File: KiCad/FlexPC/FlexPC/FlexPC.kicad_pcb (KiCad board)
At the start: 2 copper layers, 14.8 x 14.5 mm, 3 parts, among them J1 Conn_01x28, J2 Conn_01x20, J3 Conn_01x08

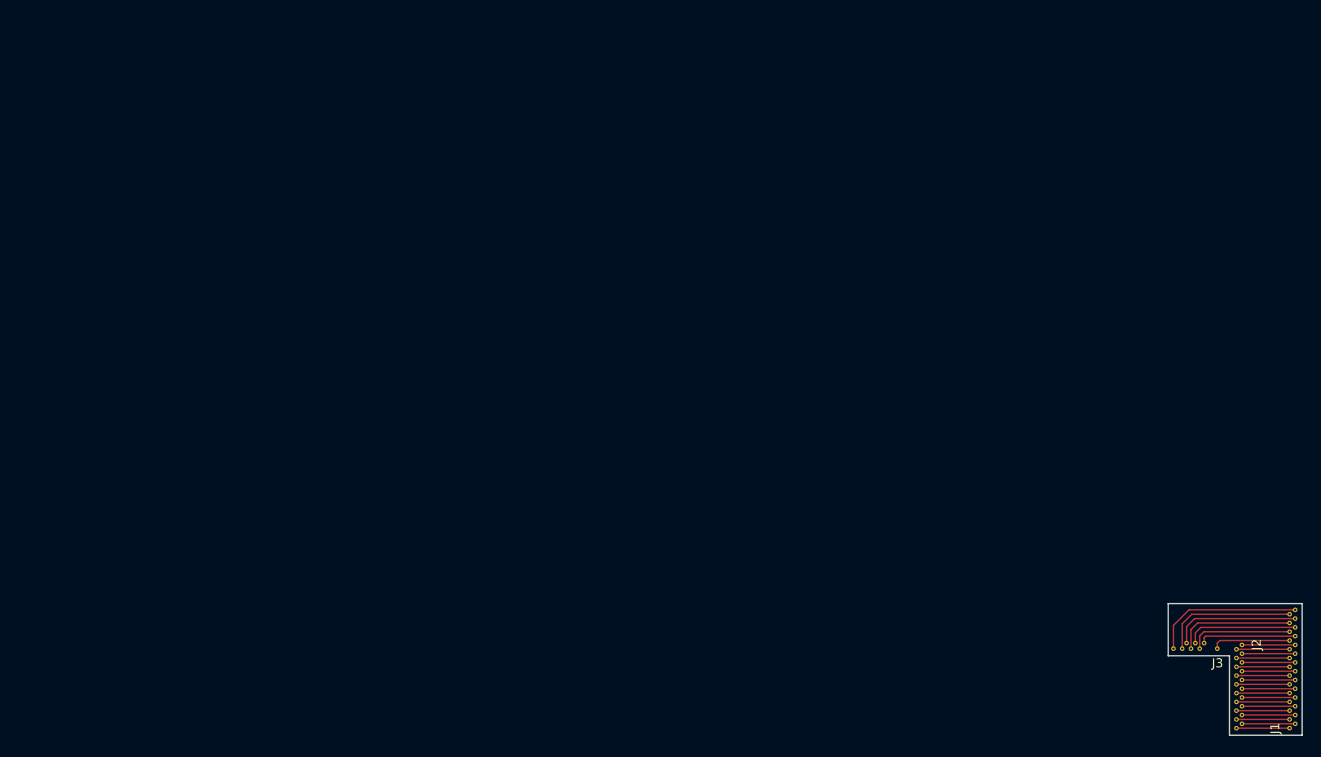
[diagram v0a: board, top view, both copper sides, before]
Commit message: FlexPC Cable
1. FlexPC Cable Generated
2. Via-trace distances are now 5 mils minimum
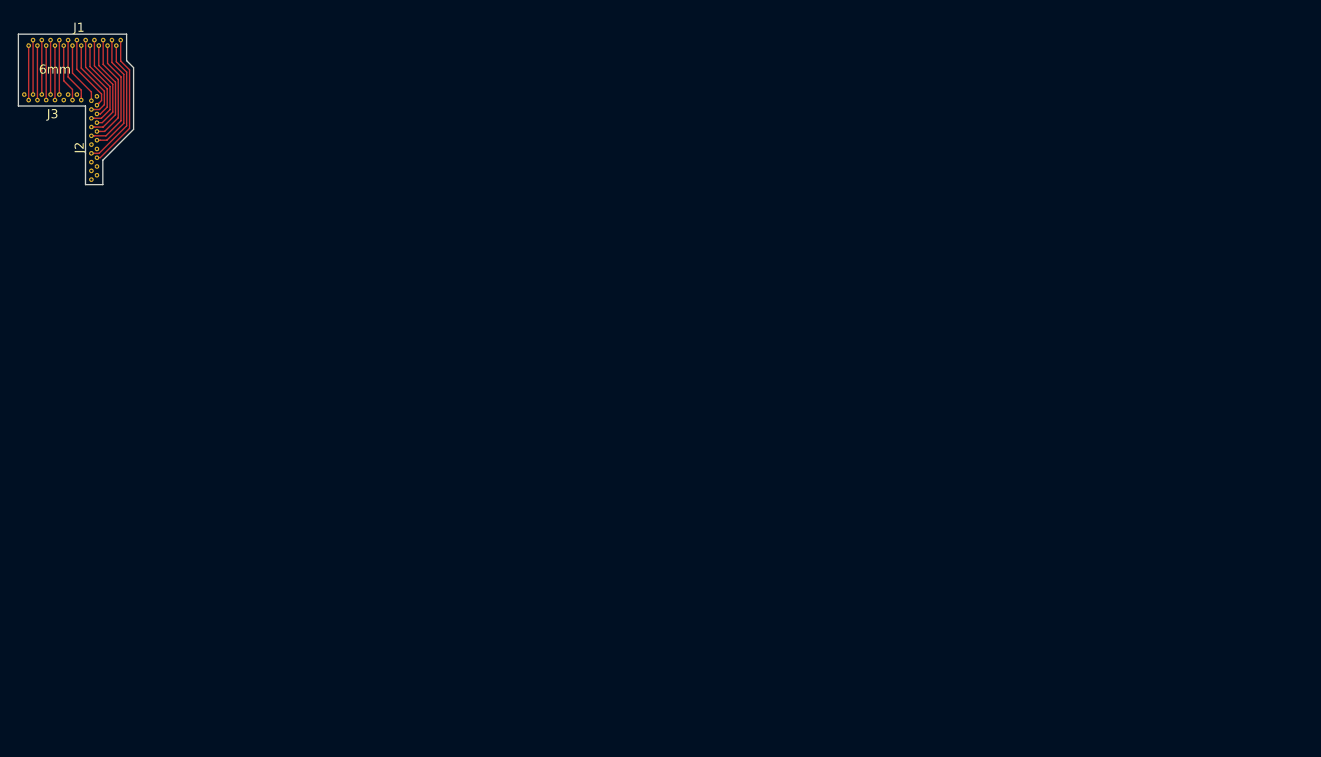
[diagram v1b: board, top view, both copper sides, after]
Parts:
- J1: value Conn_01x28 -> Conn_01x22; footprint .Connector:B2B_Flex_28_Dual_Row_38milx24mil_Hole_10milx20mil -> .Connector:B2B_Flex_22_Dual_Row_38milx24mil_Hole_10milx20mil
- J3: value Conn_01x08 -> Conn_01x14; footprint .Connector:B2B_Flex_08_Dual_Row_38milx24mil_Hole_10milx20mil -> .Connector:B2B_Flex_14_Dual_Row_38milx24mil_Hole_10milx20mil
- moved J1 149.4 mm to (37.9, 22.2), turned to 180 degrees
- moved J3 144.9 mm to (27.3, 28.2), turned to 0 degrees
- moved J2 139.8 mm to (35.3, 28.4)
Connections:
- J1 pad 1: Net-(J1-Pad1) -> /LINE_VALID
- J1 pad 10: /img_d7 -> /img_d2
- J1 pad 11: /img_d6 -> /img_d0
- J1 pad 12: Net-(J1-Pad12) -> /1V8
- J1 pad 13: Net-(J1-Pad13) -> /GND
- J1 pad 14: /FRAME_VALID -> /SS_N
- J1 pad 15: /LINE_VALID -> /SCK
- J1 pad 16: Net-(J1-Pad16) -> /RESET_N
- J1 pad 17: Net-(J1-Pad17) -> /TRIGGER0
- J1 pad 18: Net-(J1-Pad18) -> /MONITOR0
- J1 pad 19: Net-(J1-Pad19) -> /MISO
- J1 pad 2: Net-(J1-Pad2) -> /FRAME_VALID
- J1 pad 20: Net-(J1-Pad20) -> /MOSI
- J1 pad 21: /SS_N -> /3V3
- J1 pad 22: /SCK -> /Status_LED
- J1 pad 3: /img_d0 -> /img_d6
- J1 pad 4: /img_d2 -> /img_d7
- J1 pad 5: /img_d1 -> /img_d5
- J1 pad 6: /img_d3 -> /img_d4
- J1 pad 8: /img_d4 -> /img_d3
- J1 pad 9: /img_d5 -> /img_d1
- J2 pad 1: Net-(J1-Pad20) -> Net-(J2-Pad1)
- J2 pad 10: /img_d6 -> /img_d7
- J2 pad 11: /img_d7 -> /img_d6
- J2 pad 12: /img_d5 -> /img_d8
- J2 pad 13: /img_d4 -> /img_d9
- J2 pad 14: /CLK_OUT -> /FRAME_VALID
- J2 pad 15: /img_d3 -> /LINE_VALID
- J2 pad 16: /img_d1 -> Net-(J2-Pad16)
- J2 pad 17: /img_d2 -> Net-(J2-Pad17)
- J2 pad 18: /img_d0 -> Net-(J2-Pad18)
- J2 pad 19: Net-(J1-Pad2) -> Net-(J2-Pad19)
- J2 pad 2: Net-(J1-Pad19) -> /1V8
- J2 pad 20: Net-(J1-Pad1) -> Net-(J2-Pad20)
- J2 pad 3: Net-(J1-Pad18) -> /img_d0
- J2 pad 4: Net-(J1-Pad17) -> /img_d2
- J2 pad 5: Net-(J1-Pad16) -> /img_d1
- J2 pad 6: /LINE_VALID -> /img_d3
- J2 pad 7: /FRAME_VALID -> /CLK_OUT
- J2 pad 8: Net-(J1-Pad13) -> /img_d4
- J2 pad 9: Net-(J1-Pad12) -> /img_d5
- J3 pad 1: /SS_N -> /VBATT
- J3 pad 2: /SCK -> /Status_LED
- J3 pad 3: /RESET_N -> /3V3
- J3 pad 4: /TRIGGER0 -> /MOSI
- J3 pad 5: /MONITOR0 -> /MISO
- J3 pad 6: /MISO -> /MONITOR0
- J3 pad 7: /MOSI -> /TRIGGER0
- J3 pad 8: /Status_LED -> /RESET_N
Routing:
- net /Status_LED: track 16.7 -> 6.00 mm
- net /LINE_VALID: track 5.86 -> 15.1 mm
- net /MOSI: track 15.0 -> 6.00 mm
- net /FRAME_VALID: track 5.86 -> 14.4 mm
- net /MISO: track 14.1 -> 6.00 mm
- net /img_d6: track 5.86 -> 13.4 mm
- net /MONITOR0: track 13.3 -> 6.00 mm
- net /GND: track 0.00 -> 7.21 mm
- net /img_d7: track 5.86 -> 12.8 mm
- net /1V8: track 0.00 -> 6.94 mm
- net /TRIGGER0: track 12.4 -> 6.00 mm
- net /img_d5: track 5.86 -> 12.2 mm
- net /3V3: track 0.00 -> 6.00 mm
- net Net-(J1-Pad20): track 5.86 -> 0.00 mm
- net Net-(J1-Pad2): track 5.86 -> 0.00 mm
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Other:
- board size 14.8 x 14.5 mm -> 12.7 x 16.6 mm
- board text added: "6mm"
